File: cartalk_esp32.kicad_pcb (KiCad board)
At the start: 2 copper layers, 21.3 x 48.8 mm, 22 parts, among them IC1 CP2104, J1 10118192-0002LF, Q1 mmbt2222, Q2 mmbt2222, SW2 KMR2, U1 HUB75 Connector Female, U2 AP2112-3.3, X2 ESP32_WROOM32_SKINNY

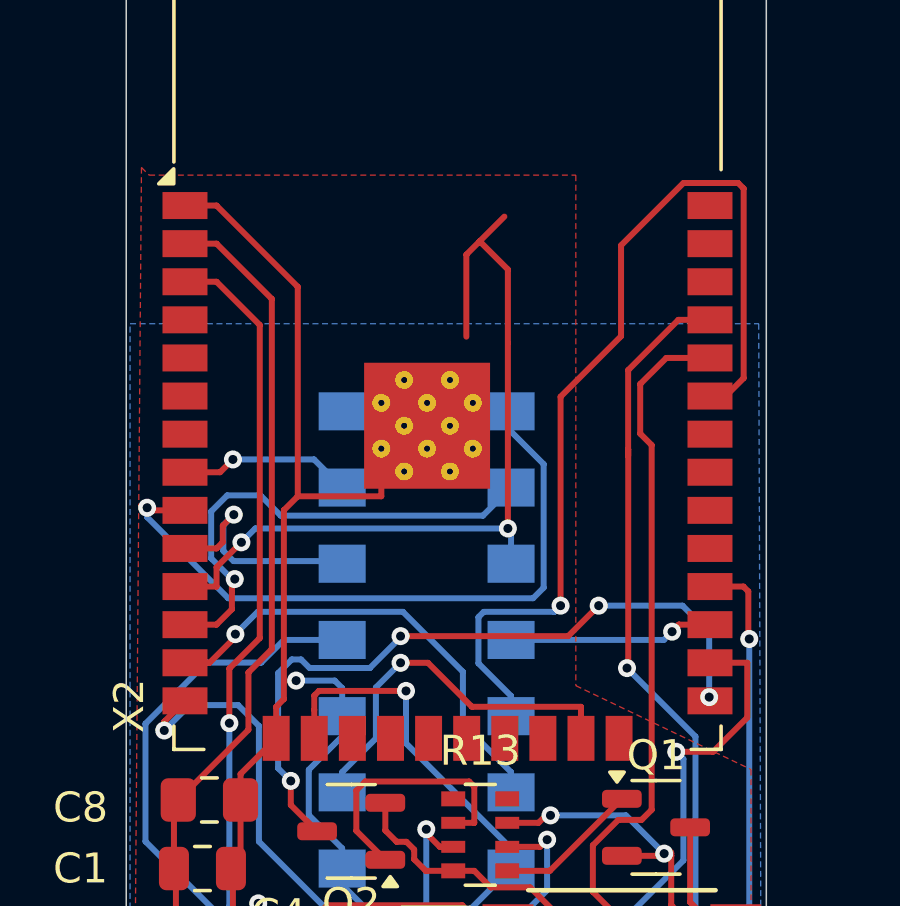
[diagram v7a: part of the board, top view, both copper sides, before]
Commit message: Remove ground plane fingers.
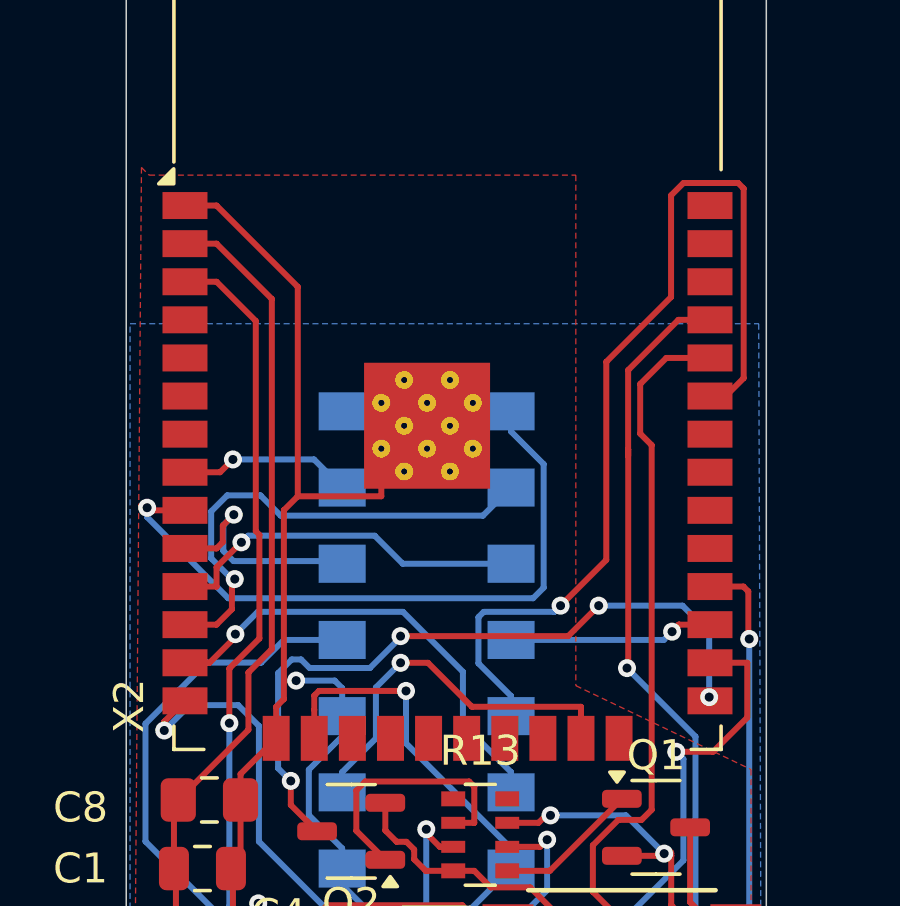
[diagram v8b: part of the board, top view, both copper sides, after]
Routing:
- net /ADDR_C: track 27.7 -> 12.4 mm, vias 2 -> 1
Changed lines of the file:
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@@
+	)
+	(segment
+		(start 123.19 93.508)
+		(end 123.19 100.516371)
+		(width 0.2)
+		(layer "F.Cu")
+		(net 3)
 	)
 	(segment
@@
 	)
 	(segment
-		(start 123.323 93.6414)
-		(end 123.323 104.078)
-		(width 0.2)
-		(layer "F.Cu")
-		(net 3)
-	)
-	(segment
-		(start 121.882 92.2)
-		(end 123.323 93.6414)
+		(start 123.19 100.516371)
+		(end 123.3111 100.637471)
 		(width 0.2)
 		(layer "F.Cu")
@@
 	)
 	(segment
-		(start 123.323 104.078)
-		(end 122.309 105.092)
+		(start 120.83 92.2)
+		(end 121.882 92.2)
 		(width 0.2)
 		(layer "F.Cu")
@@
 	)
 	(segment
+		(start 121.882 92.2)
+		(end 123.19 93.508)
+		(width 0.2)
+		(layer "F.Cu")
+		(net 3)
+	)
+	(segment
 		(start 131.597 114.052)
 		(end 131.597 113.704)
@@
 	)
 	(segment
-		(start 122.309 105.092)
-		(end 122.309 106.911)
+		(start 123.3111 104.0899)
+		(end 122.309 105.092)
 		(width 0.2)
 		(layer "F.Cu")
@@
 	)
 	(segment
-		(start 122.309 106.911)
+		(start 122.309 105.092)
 		(end 122.309 106.9142)
 		(width 0.2)
@@
 	)
 	(segment
-		(start 120.83 92.2)
-		(end 121.882 92.2)
+		(start 123.3111 100.637471)
+		(end 123.3111 104.0899)
 		(width 0.2)
 		(layer "F.Cu")
@@
 	)
 	(segment
-		(start 131.477 90.0282)
-		(end 130.654 90.8506)
-		(width 0.2)
-		(layer "F.Cu")
-		(net 34)
-	)
-	(segment
-		(start 130.209 91.2961)
-		(end 130.209 94.0306)
-		(width 0.2)
-		(layer "F.Cu")
-		(net 34)
-	)
-	(segment
 		(start 120.83 102.36)
 		(end 121.882 102.36)
@@
 	)
 	(segment
-		(start 130.654 90.8506)
-		(end 130.209 91.2961)
-		(width 0.2)
-		(layer "F.Cu")
-		(net 34)
-	)
-	(segment
-		(start 131.594 94.234)
-		(end 131.594 100.4238)
-		(width 0.2)
-		(layer "F.Cu")
-		(net 34)
-	)
-	(segment
 		(start 122.708 100.886)
 		(end 122.708 100.808)
@@
 	)
 	(segment
-		(start 130.654 90.8506)
-		(end 130.655 90.8506)
-		(width 0.2)
-		(layer "F.Cu")
-		(net 34)
-	)
-	(segment
-		(start 131.594 91.79)
-		(end 131.594 94.234)
-		(width 0.2)
-		(layer "F.Cu")
-		(net 34)
-	)
-	(segment
-		(start 130.655 90.8506)
-		(end 131.594 91.79)
-		(width 0.2)
-		(layer "F.Cu")
-		(net 34)
-	)
-	(segment
 		(start 122.708 100.886)
 		(end 122.7111 100.886)
@@
 	)
 	(via
-		(at 131.594 100.4238)
+		(at 122.7111 100.886)
 		(size 0.6)
 		(drill 0.3)
@@
 		(net 34)
 	)
-	(via
-		(at 122.7111 100.886)
-		(size 0.6)
-		(drill 0.3)
-		(layers "F.Cu" "B.Cu")
+	(segment
+		(start 127.154 100.665)
+		(end 122.9321 100.665)
+		(width 0.2)
+		(layer "B.Cu")
 		(net 34)
 	)
 	(segment
+		(start 122.9321 100.665)
+		(end 122.7111 100.886)
+		(width 0.2)
+		(layer "B.Cu")
+		(net 34)
+	)
+	(segment
+		(start 128.089 101.6)
+		(end 127.154 100.665)
+		(width 0.2)
+		(layer "B.Cu")
+		(net 34)
+	)
+	(segment
 		(start 131.699 101.6)
-		(end 131.699 100.5288)
-		(width 0.2)
-		(layer "B.Cu")
-		(net 34)
-	)
-	(segment
-		(start 123.1733 100.4238)
-		(end 122.7111 100.886)
-		(width 0.2)
-		(layer "B.Cu")
-		(net 34)
-	)
-	(segment
-		(start 131.699 100.5288)
-		(end 131.594 100.4238)
-		(width 0.2)
-		(layer "B.Cu")
-		(net 34)
-	)
-	(segment
-		(start 131.594 100.4238)
-		(end 123.1733 100.4238)
+		(end 128.089 101.6)
 		(width 0.2)
 		(layer "B.Cu")
@@
 	)
 	(segment
-		(start 133.35 102.997)
-		(end 133.35 96.0322)
-		(width 0.2)
-		(layer "F.Cu")
-		(net 39)
-	)
-	(segment
 		(start 139.269 88.9083)
 		(end 139.453 89.0923)
@@
 	)
 	(segment
-		(start 135.366 90.9878)
-		(end 137.446 88.9083)
+		(start 134.874 94.869)
+		(end 137.033 92.71)
+		(width 0.2)
+		(layer "F.Cu")
+		(net 39)
+	)
+	(segment
+		(start 137.033 92.71)
+		(end 137.033 89.3213)
+		(width 0.2)
+		(layer "F.Cu")
+		(net 39)
+	)
+	(segment
+		(start 133.35 102.997)
+		(end 134.874 101.473)
 		(width 0.2)
 		(layer "F.Cu")
@@
 	)
 	(segment
+		(start 139.453 95.4126)
+		(end 138.856 96.01)
+		(width 0.2)
+		(layer "F.Cu")
+		(net 39)
+	)
+	(segment
 		(start 139.453 89.0923)
 		(end 139.453 95.4126)
@@
 	)
 	(segment
-		(start 133.35 96.0322)
-		(end 135.366 94.0165)
+		(start 134.874 101.473)
+		(end 134.874 94.869)
 		(width 0.2)
 		(layer "F.Cu")
@@
 	)
 	(segment
-		(start 139.453 95.4126)
-		(end 138.856 96.01)
-		(width 0.2)
-		(layer "F.Cu")
-		(net 39)
-	)
-	(segment
-		(start 135.366 94.0165)
-		(end 135.366 90.9878)
+		(start 137.033 89.3213)
+		(end 137.446 88.9083)
 		(width 0.2)
 		(layer "F.Cu")
@@
 		(layer "F.Cu")
 		(net 59)
+	)
+	(zone
+		(net 0)
+		(net_name "")
+		(layer "F.Cu")
+		(hatch edge 0.5)
+		(connect_pads
+			(clearance 0)
+		)
+		(min_thickness 0.25)
+		(filled_areas_thickness no)
+		(keepout
+			(tracks allowed)
+			(vias allowed)
+			(pads allowed)
+			(copperpour not_allowed)
+			(footprints allowed)
+		)
+		(fill
+			(thermal_gap 0.5)
+			(thermal_bridge_width 0.5)
+		)
+		(polygon
+			(pts
+				(xy 140.716 113.792) (xy 137.795 113.665) (xy 137.922 117.094) (xy 137.922 117.475) (xy 140.462 117.475)
+			)
+		)
+	)
+	(zone
+		(net 0)
+		(net_name "")
+		(layer "F.Cu")
+		(hatch edge 0.5)
+		(connect_pads
+			(clearance 0)
+		)
+		(min_thickness 0.25)
+		(filled_areas_thickness no)
+		(keepout
+			(tracks allowed)
+			(vias allowed)
+			(pads allowed)
+			(copperpour not_allowed)
+			(footprints allowed)
+		)
+		(fill
+			(thermal_gap 0.5)
+			(thermal_bridge_width 0.5)
+		)
+		(polygon
+			(pts
+				(xy 118.872 99.949) (xy 118.872 116.967) (xy 121.285 116.967) (xy 121.666 108.585) (xy 122.555 107.442)
+				(xy 122.682 99.568)
+			)
+		)
 	)
 	(zone
@@
 		(polygon
 			(pts
-				(xy 130.81 93.218) (xy 130.81 99.695) (xy 132.842 103.251) (xy 136.779 107.442) (xy 136.271 111.887)
-				(xy 133.35 113.919) (xy 128.841 115.824) (xy 125.918 119.7665) (xy 119.126 119.634) (xy 113.792 124.587)
+				(xy 130.81 93.218) (xy 130.81 99.695) (xy 132.842 103.251) (xy 132.969 112.903) (xy 139.954 114.935)
+				(xy 141.478 120.142) (xy 142.24 131.064) (xy 135.001 130.683) (xy 133.858 122.555) (xy 113.792 124.587)
 				(xy 118.11 133.477) (xy 145.034 133.477) (xy 146.431 116.332) (xy 142.875 92.583)
 			)
